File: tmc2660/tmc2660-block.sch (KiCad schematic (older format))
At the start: 16 parts, among them J1 0R, P3 Motor, U1 TMC2660

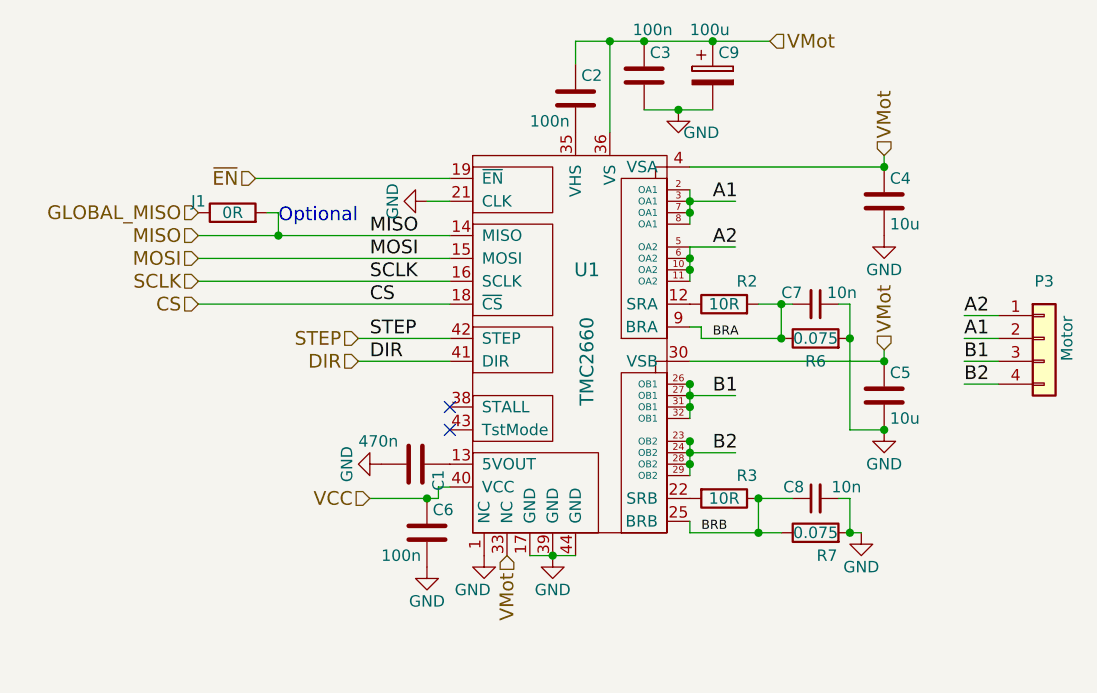
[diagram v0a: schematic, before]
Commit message: More sensible annotations, starting in the 100 range.
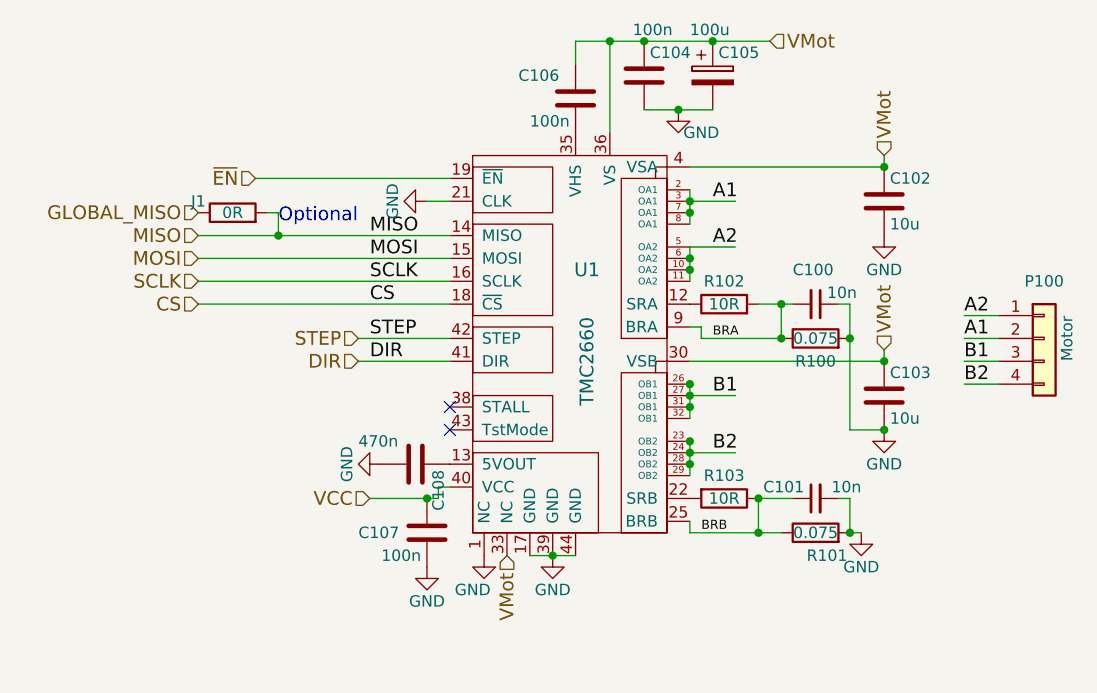
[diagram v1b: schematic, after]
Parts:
- renumbered C7 to C100, C8 to C101, C4 to C102, C5 to C103, C3 to C104, C9 to C105, C2 to C106, C6 to C107, C1 to C108, P3 to P100, R6 to R100, R7 to R101, R2 to R102, R3 to R103
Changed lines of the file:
@@
 $EndDescr
 $Comp
-L device:C C4
+L device:C C102
 U 1 1 5A0CA5B9
 P 4250 2250
-F 0 "C4" H 4275 2350 50  0000 L CNN
+F 0 "C102" H 4275 2350 50  0000 L CNN
 F 1 "10u" H 4275 2150 50  0000 L CNN
 F 2 "Capacitors_SMD:C_1206" H 4288 2100 30  0001 C CNN
@@
 $EndComp
 $Comp
-L device:C C5
+L device:C C103
 U 1 1 5A0CA5C0
 P 4250 3100
-F 0 "C5" H 4275 3200 50  0000 L CNN
+F 0 "C103" H 4275 3200 50  0000 L CNN
 F 1 "10u" H 4275 3000 50  0000 L CNN
 F 2 "Capacitors_SMD:C_1206" H 4288 2950 30  0001 C CNN
@@
 $EndComp
 $Comp
-L device:C C2
+L device:C C106
 U 1 1 5A0CA5D3
 P 2900 1800
-F 0 "C2" H 2925 1900 50  0000 L CNN
+F 0 "C106" H 2650 1900 50  0000 L CNN
 F 1 "100n" H 2700 1700 50  0000 L CNN
 F 2 "Capacitors_SMD:C_0805" H 2938 1650 30  0001 C CNN
@@
 	3400 2100 4250 2100
 $Comp
-L device:C C3
+L device:C C104
 U 1 1 5A0CA5DE
 P 3200 1700
-F 0 "C3" H 3225 1800 50  0000 L CNN
+F 0 "C104" H 3225 1800 50  0000 L CNN
 F 1 "100n" H 3150 1900 50  0000 L CNN
 F 2 "Capacitors_SMD:C_0805" H 3238 1550 30  0001 C CNN
@@
 Connection ~ 3400 3150
 $Comp
-L device:R R2
+L device:R R102
 U 1 1 5A0CA5F8
 P 3550 2700
-F 0 "R2" V 3650 2600 50  0000 C CNN
+F 0 "R102" V 3650 2700 50  0000 C CNN
 F 1 "10R" V 3550 2700 50  0000 C CNN
 F 2 "Resistors_SMD:R_0603" V 3480 2700 30  0001 C CNN
@@
 $EndComp
 $Comp
-L device:R R3
+L device:R R103
 U 1 1 5A0CA5FF
 P 3550 3550
-F 0 "R3" V 3450 3650 50  0000 C CNN
+F 0 "R103" V 3450 3550 50  0000 C CNN
 F 1 "10R" V 3550 3550 50  0000 C CNN
 F 2 "Resistors_SMD:R_0603" V 3480 3550 30  0001 C CNN
@@
 	3400 2250 3600 2250
 $Comp
-L Connector:Conn_01x04 P3
+L Connector:Conn_01x04 P100
 U 1 1 5A0CA611
 P 4950 2850
-F 0 "P3" H 4950 3100 50  0000 C CNN
+F 0 "P100" H 4950 3100 50  0000 C CNN
 F 1 "Motor" V 5050 2850 50  0000 C CNN
 F 2 "Connectors_JST:JST_XH_B04B-XH-A_04x2.50mm_Straight" H 4950 2850 60  0001 C CNN
@@
 $EndComp
 $Comp
-L device:C C1
+L device:C C108
 U 1 1 5A0CA61C
 P 2200 3400
-F 0 "C1" H 2225 3500 50  0000 L CNN
+F 0 "C108" H 2225 3500 50  0000 L CNN
 F 1 "470n" V 2100 3150 50  0000 L CNN
 F 2 "Capacitors_SMD:C_0603" H 2238 3250 30  0001 C CNN
@@
 $EndComp
 $Comp
-L device:C C6
+L device:C C107
 U 1 1 5A0CA648
 P 2250 3700
-F 0 "C6" H 2275 3800 50  0000 L CNN
+F 0 "C107" H 1950 3700 50  0000 L CNN
 F 1 "100n" H 2050 3600 50  0000 L CNN
 F 2 "Capacitors_SMD:C_0603" H 2288 3550 30  0001 C CNN
@@
 $EndComp
 $Comp
-L device:R R7
+L device:R R101
 U 1 1 5A0CA66C
 P 3950 3700
-F 0 "R7" V 3850 3650 50  0000 C CNN
+F 0 "R101" V 3850 3650 50  0000 C CNN
 F 1 "0.075" V 3950 3700 50  0000 C CNN
 F 2 "Resistors_SMD:R_2512" V 3880 3700 30  0001 C CNN
@@
 $EndComp
 $Comp
-L device:R R6
+L device:R R100
 U 1 1 5A0CA673
 P 3950 2850
-F 0 "R6" V 3850 2850 50  0000 C CNN
+F 0 "R100" V 3850 2850 50  0000 C CNN
 F 1 "0.075" V 3950 2850 50  0000 C CNN
 F 2 "Resistors_SMD:R_2512" V 3880 2850 30  0001 C CNN
@@
 	2250 2250 2350 2250
 $Comp
-L device:C_Small C7
+L device:C_Small C100
 U 1 1 5A0CA67B
 P 3950 2700
-F 0 "C7" V 3900 2550 50  0000 L CNN
+F 0 "C100" V 3800 2600 50  0000 L CNN
 F 1 "10n" V 3900 2750 50  0000 L CNN
 F 2 "Capacitors_SMD:C_0603" H 3988 2550 30  0001 C CNN
@@
 	3400 2450 3600 2450
 $Comp
-L device:C_Small C8
+L device:C_Small C101
 U 1 1 5A0CA683
 P 3950 3550
-F 0 "C8" V 4000 3600 50  0000 L CNN
+F 0 "C101" V 4000 3600 50  0000 L CNN
 F 1 "10n" V 4000 3350 50  0000 L CNN
 F 2 "Capacitors_SMD:C_0603" H 3988 3400 30  0001 C CNN
@@
 Connection ~ 3800 2700
 $Comp
-L device:CP C9
+L device:CP C105
 U 1 1 5A0CA6BD
 P 3500 1700
-F 0 "C9" H 3525 1800 50  0000 L CNN
+F 0 "C105" H 3525 1800 50  0000 L CNN
 F 1 "100u" H 3400 1900 50  0000 L CNN
 F 2 "Capacitors_THT:CP_Radial_D10.0mm_P5.00mm" H 3538 1550 30  0001 C CNN

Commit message: Numbering scheme: have U1 be U100.
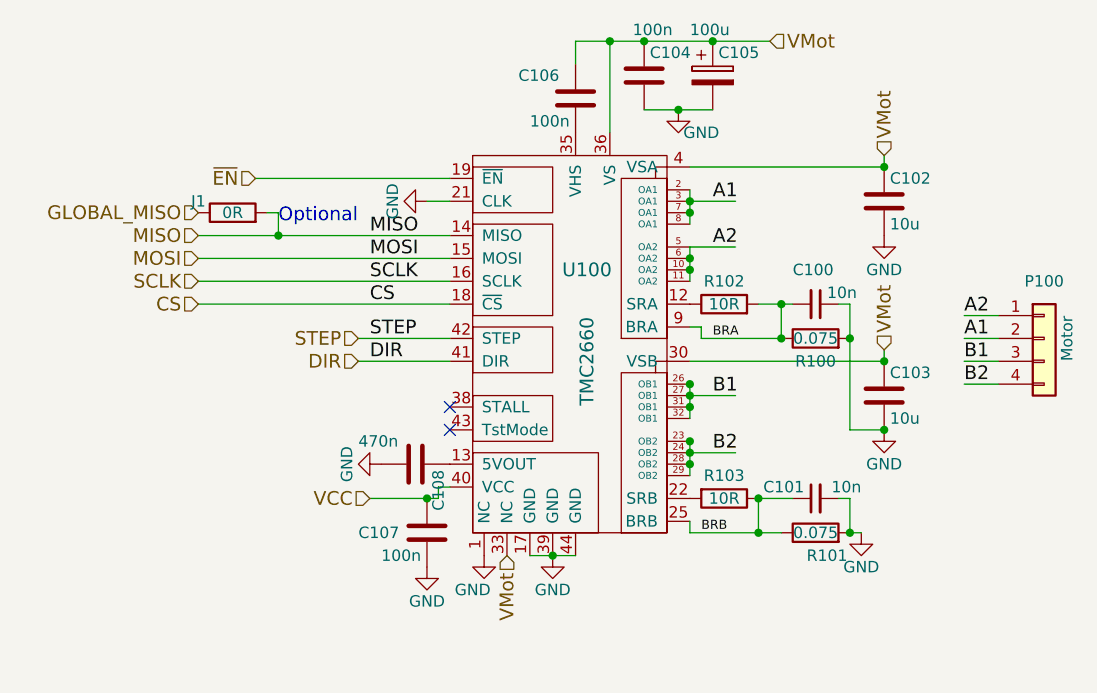
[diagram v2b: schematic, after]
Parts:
- renumbered U1 to U100
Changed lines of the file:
@@
 $EndComp
 $Comp
-L power:GND #PWR01
+L power:GND #PWR101
 U 1 1 5A0CA5C7
 P 4250 3250
-F 0 "#PWR01" H 4250 3000 50  0001 C CNN
+F 0 "#PWR101" H 4250 3000 50  0001 C CNN
 F 1 "GND" H 4250 3100 50  0000 C CNN
 F 2 "" H 4250 3250 60  0000 C CNN
@@
 $EndComp
 $Comp
-L power:GND #PWR02
+L power:GND #PWR102
 U 1 1 5A0CA5CD
 P 4250 2400
-F 0 "#PWR02" H 4250 2150 50  0001 C CNN
+F 0 "#PWR102" H 4250 2150 50  0001 C CNN
 F 1 "GND" H 4250 2250 50  0000 C CNN
 F 2 "" H 4250 2400 60  0000 C CNN
@@
 Connection ~ 3050 1550
 $Comp
-L power:GND #PWR03
+L power:GND #PWR103
 U 1 1 5A0CA5E6
 P 3350 1850
-F 0 "#PWR03" H 3350 1600 50  0001 C CNN
+F 0 "#PWR103" H 3350 1600 50  0001 C CNN
 F 1 "GND" H 3450 1750 50  0000 C CNN
 F 2 "" H 3350 1850 60  0000 C CNN
@@
 Connection ~ 2800 3800
 $Comp
-L power:GND #PWR04
+L power:GND #PWR104
 U 1 1 5A0CA5EF
 P 2800 3800
-F 0 "#PWR04" H 2800 3550 50  0001 C CNN
+F 0 "#PWR104" H 2800 3550 50  0001 C CNN
 F 1 "GND" H 2800 3650 50  0000 C CNN
 F 2 "" H 2800 3800 60  0000 C CNN
@@
 $EndComp
 $Comp
-L power:GND #PWR05
+L power:GND #PWR105
 U 1 1 5A0CA606
 P 4150 3700
-F 0 "#PWR05" H 4150 3450 50  0001 C CNN
+F 0 "#PWR105" H 4150 3450 50  0001 C CNN
 F 1 "GND" H 4150 3550 50  0000 C CNN
 F 2 "" H 4150 3700 60  0000 C CNN
@@
 $EndComp
 $Comp
-L power:GND #PWR06
+L power:GND #PWR106
 U 1 1 5A0CA623
 P 2050 3400
-F 0 "#PWR06" H 2050 3150 50  0001 C CNN
+F 0 "#PWR106" H 2050 3150 50  0001 C CNN
 F 1 "GND" H 2050 3250 50  0000 C CNN
 F 2 "" H 2050 3400 60  0000 C CNN
@@
 $EndComp
 $Comp
-L tmc2660:TMC2660 U1
+L tmc2660:TMC2660 U100
 U 1 1 5A0CA62A
 P 2950 2850
-F 0 "U1" H 2950 3150 60  0000 C CNN
+F 0 "U100" H 2950 3150 60  0000 C CNN
 F 1 "TMC2660" V 2950 2750 60  0000 C CNN
 F 2 "Housings_QFP:LQFP-44_10x10mm_Pitch0.8mm" H 3050 3450 60  0001 C CNN
@@
 Connection ~ 4250 2950
 $Comp
-L power:GND #PWR07
+L power:GND #PWR107
 U 1 1 5A0CA642
 P 2250 3850
-F 0 "#PWR07" H 2250 3600 50  0001 C CNN
+F 0 "#PWR107" H 2250 3600 50  0001 C CNN
 F 1 "GND" H 2250 3700 50  0000 C CNN
 F 2 "" H 2250 3850 60  0000 C CNN
@@
 NoConn ~ 2350 3250
 $Comp
-L power:GND #PWR08
+L power:GND #PWR108
 U 1 1 5A0CA65B
 P 2250 2250
-F 0 "#PWR08" H 2250 2000 50  0001 C CNN
+F 0 "#PWR108" H 2250 2000 50  0001 C CNN
 F 1 "GND" H 2250 2100 50  0000 C CNN
 F 2 "" H 2250 2250 60  0000 C CNN
@@
 	2300 3550 2000 3550
 $Comp
-L power:GND #PWR09
+L power:GND #PWR109
 U 1 1 5A0CA666
 P 2500 3800
-F 0 "#PWR09" H 2500 3550 50  0001 C CNN
+F 0 "#PWR109" H 2500 3550 50  0001 C CNN
 F 1 "GND" H 2450 3650 50  0000 C CNN
 F 2 "" H 2500 3800 60  0000 C CNN

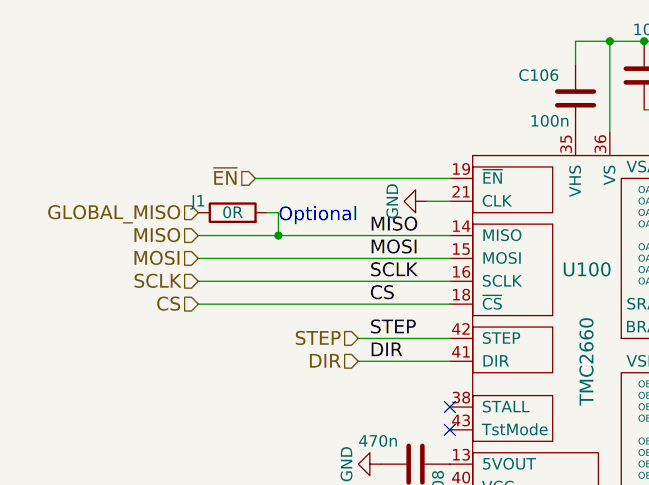
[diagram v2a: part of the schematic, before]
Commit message: J1 -> J100
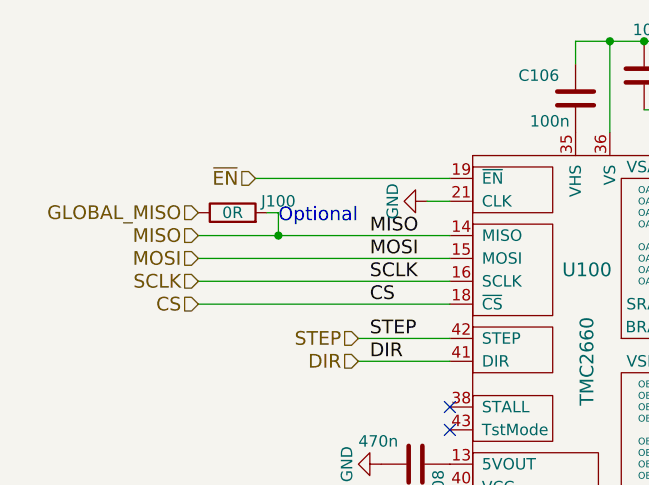
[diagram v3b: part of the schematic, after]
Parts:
- renumbered J1 to J100
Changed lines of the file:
@@
 ~EN
 $Comp
-L device:R J1
+L device:R J100
 U 1 1 5A0CA6C8
 P 1400 2300
-F 0 "J1" V 1450 2450 50  0000 C CNN
+F 0 "J100" V 1450 2100 50  0000 C CNN
 F 1 "0R" V 1400 2300 50  0000 C CNN
 F 2 "Resistors_SMD:R_0603" V 1330 2300 30  0001 C CNN

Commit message: More preparation for cloning.
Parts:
- added M100, M101: Mount, Mounting_Holes:MountingHole_2.7mm_M2.5, symbol Connector:Test_Point
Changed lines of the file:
@@
 Wire Wire Line
 	4600 3050 4750 3050
+$Comp
+L Connector:Test_Point M100
+U 1 1 5A0FBC47
+P 1250 4300
+F 0 "M100" H 1308 4420 50  0000 L CNN
+F 1 "Mount" H 1308 4329 50  0000 L CNN
+F 2 "Mounting_Holes:MountingHole_2.7mm_M2.5" H 1450 4300 50  0001 C CNN
+F 3 "~" H 1450 4300 50  0001 C CNN
+	1    1250 4300
+	1    0    0    -1
+$EndComp
+$Comp
+L Connector:Test_Point M101
+U 1 1 5A0FBD0F
+P 1650 4300
+F 0 "M101" H 1708 4420 50  0000 L CNN
+F 1 "Mount" H 1708 4329 50  0000 L CNN
+F 2 "Mounting_Holes:MountingHole_2.7mm_M2.5" H 1850 4300 50  0001 C CNN
+F 3 "~" H 1850 4300 50  0001 C CNN
+	1    1650 4300
+	1    0    0    -1
+$EndComp
 $EndSCHEMATC
